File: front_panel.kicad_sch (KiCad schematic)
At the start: 9 parts, among them SW1 SW_SPST

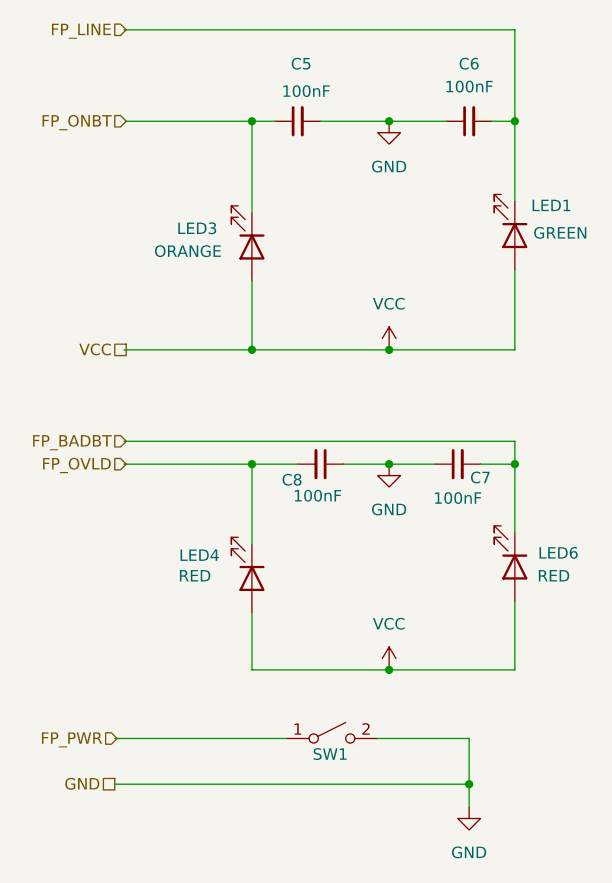
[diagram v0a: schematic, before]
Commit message: Almost all components added to schematic. Some traces and an IC missing.
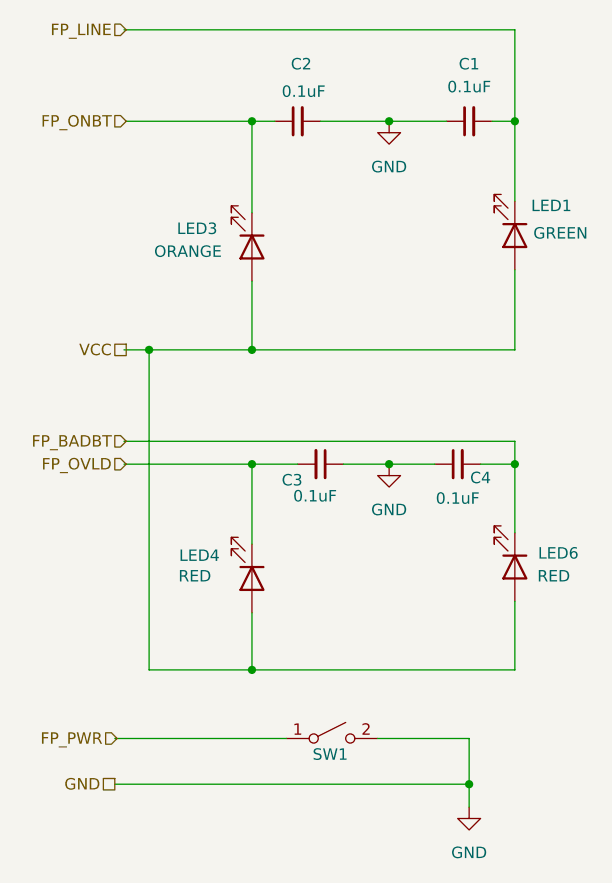
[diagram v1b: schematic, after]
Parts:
- C1: renamed from C6; value 100nF -> 0.1uF
- C2: renamed from C5; value 100nF -> 0.1uF
- C3: renamed from C8; value 100nF -> 0.1uF
- C4: renamed from C7; value 100nF -> 0.1uF
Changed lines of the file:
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@@
 	)
 	(junction
-		(at 193.04 124.46)
+		(at 177.8 124.46)
 		(diameter 0)
 		(color 0 0 0 0)
@@
 	)
 	(junction
-		(at 193.04 88.9)
-		(diameter 0)
-		(color 0 0 0 0)
-	)
-	(junction
 		(at 177.8 63.5)
 		(diameter 0)
@@
 	)
 	(junction
+		(at 166.37 88.9)
+		(diameter 0)
+		(color 0 0 0 0)
+	)
+	(junction
 		(at 177.8 101.6)
 		(diameter 0)
@@
 	(wire
 		(pts
+			(xy 166.37 88.9) (xy 166.37 124.46)
+		)
+		(stroke
+			(width 0)
+			(type default)
+		)
+	)
+	(wire
+		(pts
 			(xy 163.576 99.06) (xy 207.01 99.06)
 		)
@@
 	(wire
 		(pts
-			(xy 177.8 88.9) (xy 193.04 88.9)
-		)
-		(stroke
-			(width 0)
-			(type default)
-		)
-	)
-	(wire
-		(pts
 			(xy 177.8 63.5) (xy 177.8 73.66)
 		)
@@
 	(wire
 		(pts
-			(xy 193.04 124.46) (xy 207.01 124.46)
+			(xy 166.37 88.9) (xy 177.8 88.9)
 		)
 		(stroke
@@
 	(wire
 		(pts
-			(xy 163.576 88.9) (xy 177.8 88.9)
+			(xy 163.576 88.9) (xy 166.37 88.9)
 		)
 		(stroke
@@
 	(wire
 		(pts
+			(xy 166.37 124.46) (xy 177.8 124.46)
+		)
+		(stroke
+			(width 0)
+			(type default)
+		)
+	)
+	(wire
+		(pts
 			(xy 177.8 81.28) (xy 177.8 88.9)
 		)
@@
 	(wire
 		(pts
-			(xy 193.04 88.9) (xy 207.01 88.9)
-		)
-		(stroke
-			(width 0)
-			(type default)
-		)
-	)
-	(wire
-		(pts
-			(xy 177.8 124.46) (xy 193.04 124.46)
+			(xy 177.8 88.9) (xy 207.01 88.9)
+		)
+		(stroke
+			(width 0)
+			(type default)
+		)
+	)
+	(wire
+		(pts
+			(xy 177.8 124.46) (xy 207.01 124.46)
 		)
 		(stroke
@@
 		(on_board yes)
 		(dnp no)
-		(property "Reference" "C8"
+		(property "Reference" "C3"
 			(at 181.102 103.378 90)
 			(effects
@@
 			)
 		)
-		(property "Value" "100nF"
+		(property "Value" "0.1uF"
 			(at 182.372 105.156 90)
 			(effects
@@
 			(project "pcb"
 				(path "/aee32292-8cb2-4705-b52a-d45385227d25/ff3e6cba-69a3-40bd-aaa4-7902db5b54e7"
-					(reference "C8")
-					(unit 1)
-				)
-			)
-		)
-	)
-	(symbol
-		(lib_id "power:VCC")
-		(at 193.04 124.46 0)
-		(unit 1)
-		(exclude_from_sim no)
-		(in_bom yes)
-		(on_board yes)
-		(dnp no)
-		(fields_autoplaced yes)
-		(property "Reference" "#PWR05"
-			(at 193.04 128.27 0)
-			(effects
-				(font
-					(size 1.27 1.27)
-				)
-				(hide yes)
-			)
-		)
-		(property "Value" "VCC"
-			(at 193.04 119.38 0)
-			(effects
-				(font
-					(size 1.27 1.27)
-				)
-			)
-		)
-		(property "Footprint" ""
-			(at 193.04 124.46 0)
-			(effects
-				(font
-					(size 1.27 1.27)
-				)
-				(hide yes)
-			)
-		)
-		(property "Datasheet" ""
-			(at 193.04 124.46 0)
-			(effects
-				(font
-					(size 1.27 1.27)
-				)
-				(hide yes)
-			)
-		)
-		(property "Description" "Power symbol creates a global label with name \"VCC\""
-			(at 193.04 124.46 0)
-			(effects
-				(font
-					(size 1.27 1.27)
-				)
-				(hide yes)
-			)
-		)
-		(pin "1"
-		)
-		(instances
-			(project "pcb"
-				(path "/aee32292-8cb2-4705-b52a-d45385227d25/ff3e6cba-69a3-40bd-aaa4-7902db5b54e7"
-					(reference "#PWR05")
-					(unit 1)
-				)
-			)
-		)
-	)
-	(symbol
-		(lib_id "power:VCC")
-		(at 193.04 88.9 0)
-		(unit 1)
-		(exclude_from_sim no)
-		(in_bom yes)
-		(on_board yes)
-		(dnp no)
-		(fields_autoplaced yes)
-		(property "Reference" "#PWR02"
-			(at 193.04 92.71 0)
-			(effects
-				(font
-					(size 1.27 1.27)
-				)
-				(hide yes)
-			)
-		)
-		(property "Value" "VCC"
-			(at 193.04 83.82 0)
-			(effects
-				(font
-					(size 1.27 1.27)
-				)
-			)
-		)
-		(property "Footprint" ""
-			(at 193.04 88.9 0)
-			(effects
-				(font
-					(size 1.27 1.27)
-				)
-				(hide yes)
-			)
-		)
-		(property "Datasheet" ""
-			(at 193.04 88.9 0)
-			(effects
-				(font
-					(size 1.27 1.27)
-				)
-				(hide yes)
-			)
-		)
-		(property "Description" "Power symbol creates a global label with name \"VCC\""
-			(at 193.04 88.9 0)
-			(effects
-				(font
-					(size 1.27 1.27)
-				)
-				(hide yes)
-			)
-		)
-		(pin "1"
-		)
-		(instances
-			(project ""
-				(path "/aee32292-8cb2-4705-b52a-d45385227d25/ff3e6cba-69a3-40bd-aaa4-7902db5b54e7"
-					(reference "#PWR02")
+					(reference "C3")
 					(unit 1)
 				)
@@
 		(dnp no)
 		(fields_autoplaced yes)
-		(property "Reference" "C6"
+		(property "Reference" "C1"
 			(at 201.9363 57.15 90)
 			(effects
@@
 			)
 		)
-		(property "Value" "100nF"
+		(property "Value" "0.1uF"
 			(at 201.9363 59.69 90)
 			(effects
@@
 			(project "pcb"
 				(path "/aee32292-8cb2-4705-b52a-d45385227d25/ff3e6cba-69a3-40bd-aaa4-7902db5b54e7"
-					(reference "C6")
+					(reference "C1")
 					(unit 1)
 				)
@@
 		(on_board yes)
 		(dnp no)
-		(property "Reference" "C5"
+		(property "Reference" "C2"
 			(at 182.118 57.15 90)
 			(effects
@@
 			)
 		)
-		(property "Value" "100nF"
+		(property "Value" "0.1uF"
 			(at 181.102 60.198 90)
 			(effects
@@
 			(project "pcb"
 				(path "/aee32292-8cb2-4705-b52a-d45385227d25/ff3e6cba-69a3-40bd-aaa4-7902db5b54e7"
-					(reference "C5")
+					(reference "C2")
 					(unit 1)
 				)
@@
 		(on_board yes)
 		(dnp no)
-		(property "Reference" "C7"
+		(property "Reference" "C4"
 			(at 203.2 103.124 90)
 			(effects
@@
 			)
 		)
-		(property "Value" "100nF"
+		(property "Value" "0.1uF"
 			(at 200.66 105.41 90)
 			(effects
@@
 			(project "pcb"
 				(path "/aee32292-8cb2-4705-b52a-d45385227d25/ff3e6cba-69a3-40bd-aaa4-7902db5b54e7"
-					(reference "C7")
+					(reference "C4")
 					(unit 1)
 				)
